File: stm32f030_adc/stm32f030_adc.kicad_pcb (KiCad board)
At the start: 2 copper layers, 38 parts, among them Q1 BC337, U1 STM32F103C6Tx, U2 AMS1117-3.3, X1 USB_B_Micro, Y2 8 MHz

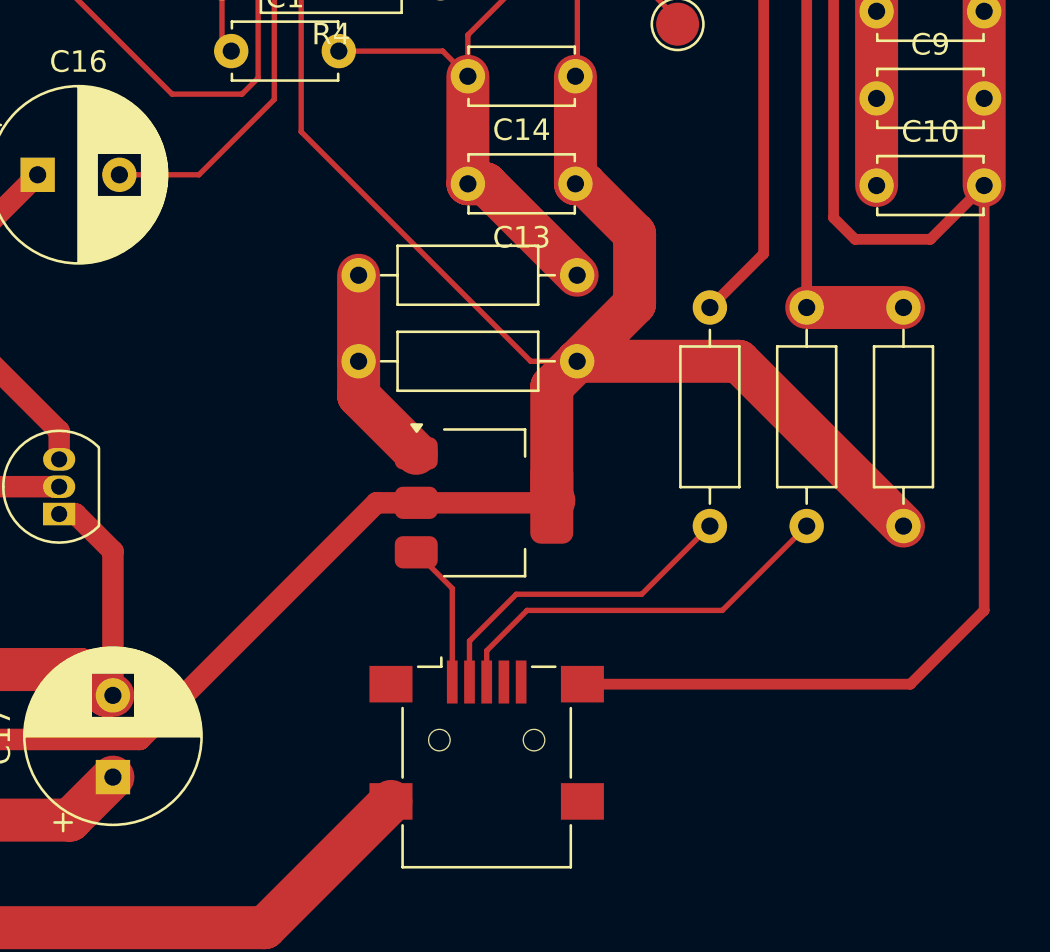
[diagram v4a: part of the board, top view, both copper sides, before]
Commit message: Layout: fixed unconnected items (except for the LDO which should not have the connection anyway)
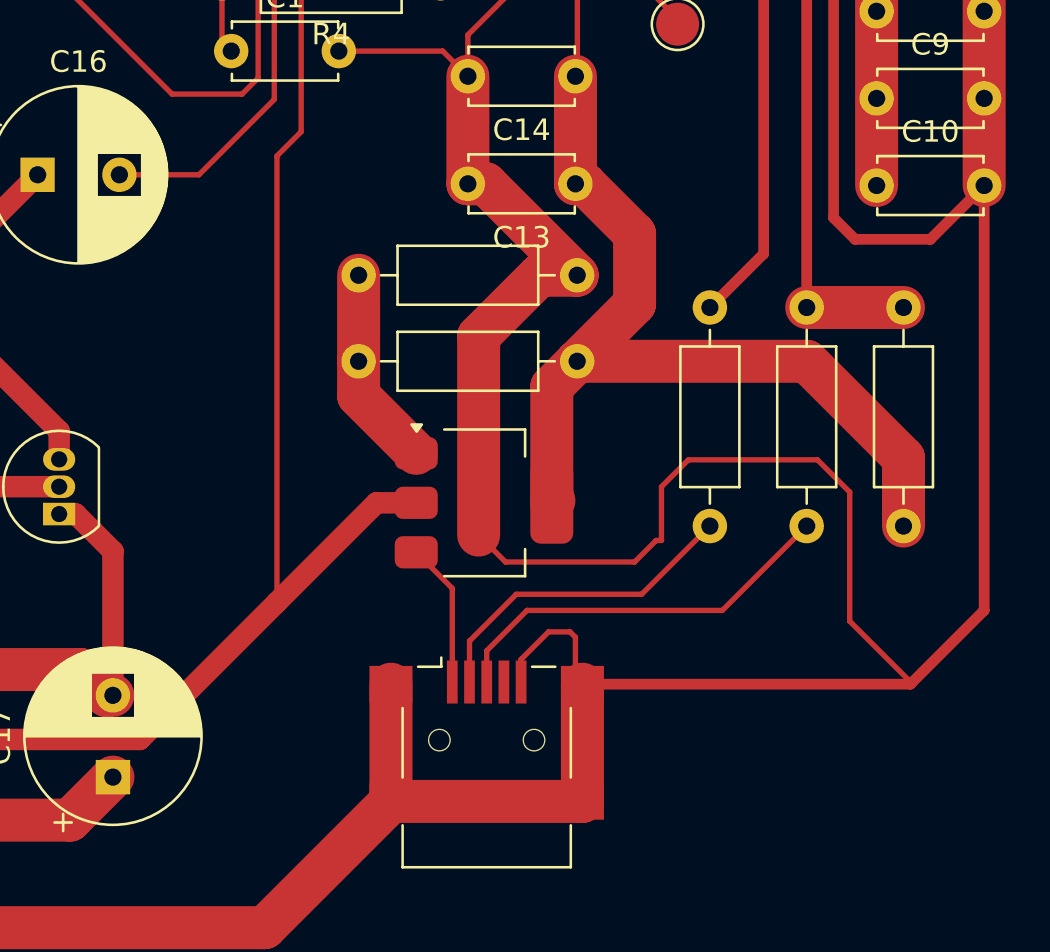
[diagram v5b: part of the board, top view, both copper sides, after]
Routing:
- net GNDREF: track 342.0 -> 415.2 mm
- net +3V3: track 221.2 -> 221.9 mm
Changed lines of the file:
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@@
 	)
 	(segment
-		(start 175.25 129.25)
-		(end 171.82 132.68)
-		(width 0.5)
+		(start 152.08 109.42)
+		(end 156.33 113.67)
+		(width 2)
 		(layer "F.Cu")
 		(net 1)
@@
 	)
 	(segment
+		(start 147.675 138.13)
+		(end 147.675 132.68)
+		(width 2)
+		(layer "F.Cu")
+		(net 1)
+	)
+	(segment
 		(start 117.552651 85.5)
 		(end 129 85.5)
@@
 	)
 	(segment
+		(start 147.675 138.13)
+		(end 156.575 138.13)
+		(width 2)
+		(layer "F.Cu")
+		(net 1)
+	)
+	(segment
 		(start 129 85.5)
 		(end 133 89.5)
@@
 	)
 	(segment
+		(start 159 127)
+		(end 160 126)
+		(width 0.25)
+		(layer "F.Cu")
+		(net 1)
+	)
+	(segment
 		(start 175.25 109.5)
 		(end 175.25 129.25)
@@
 	)
 	(segment
+		(start 169 129.75)
+		(end 171.875 132.625)
+		(width 0.25)
+		(layer "F.Cu")
+		(net 1)
+	)
+	(segment
 		(start 137.5 105.25)
 		(end 140.75 105.25)
@@
 	)
 	(segment
+		(start 160.25 126)
+		(end 160.25 123.5)
+		(width 0.25)
+		(layer "F.Cu")
+		(net 1)
+	)
+	(segment
+		(start 153.725 131.525)
+		(end 155 130.25)
+		(width 0.25)
+		(layer "F.Cu")
+		(net 1)
+	)
+	(segment
 		(start 141.5 104.5)
 		(end 141.5 98.5)
@@
 	)
 	(segment
+		(start 151.75 125.75)
+		(end 153 127)
+		(width 0.25)
+		(layer "F.Cu")
+		(net 1)
+	)
+	(segment
+		(start 153 127)
+		(end 159 127)
+		(width 0.25)
+		(layer "F.Cu")
+		(net 1)
+	)
+	(segment
+		(start 155 130.25)
+		(end 156 130.25)
+		(width 0.25)
+		(layer "F.Cu")
+		(net 1)
+	)
+	(segment
+		(start 151.25 109.42)
+		(end 152.08 109.42)
+		(width 2)
+		(layer "F.Cu")
+		(net 1)
+	)
+	(segment
 		(start 164.25 68.75)
 		(end 173.75 68.75)
@@
 	)
 	(segment
+		(start 171.875 132.625)
+		(end 171.82 132.68)
+		(width 0.5)
+		(layer "F.Cu")
+		(net 1)
+	)
+	(segment
+		(start 156.25 132.355)
+		(end 156.575 132.68)
+		(width 0.25)
+		(layer "F.Cu")
+		(net 1)
+	)
+	(segment
 		(start 114.17 125.92)
 		(end 110 121.75)
@@
 	)
 	(segment
+		(start 156.575 138.13)
+		(end 156.575 132.68)
+		(width 2)
+		(layer "F.Cu")
+		(net 1)
+	)
+	(segment
+		(start 169 123.75)
+		(end 169 129.75)
+		(width 0.25)
+		(layer "F.Cu")
+		(net 1)
+	)
+	(segment
 		(start 163 87.5)
 		(end 166.25 87.5)
@@
 	)
 	(segment
+		(start 154.58 113.67)
+		(end 151.75 116.5)
+		(width 2)
+		(layer "F.Cu")
+		(net 1)
+	)
+	(segment
 		(start 157.75 90.25)
 		(end 160.25 90.25)
@@
 	)
 	(segment
+		(start 156.25 130.5)
+		(end 156.25 132.355)
+		(width 0.25)
+		(layer "F.Cu")
+		(net 1)
+	)
+	(segment
 		(start 141.805 144)
 		(end 147.675 138.13)
@@
 	)
 	(segment
+		(start 156.33 113.67)
+		(end 154.58 113.67)
+		(width 2)
+		(layer "F.Cu")
+		(net 1)
+	)
+	(segment
 		(start 114.17 126)
 		(end 114.17 125.92)
@@
 	)
 	(segment
-		(start 151.25 109.42)
-		(end 152.08 109.42)
-		(width 2)
+		(start 160.25 123.5)
+		(end 161.5 122.25)
+		(width 0.25)
+		(layer "F.Cu")
+		(net 1)
+	)
+	(segment
+		(start 160 126)
+		(end 160.25 126)
+		(width 0.25)
 		(layer "F.Cu")
 		(net 1)
@@
 	)
 	(segment
+		(start 175.25 129.25)
+		(end 171.875 132.625)
+		(width 0.5)
+		(layer "F.Cu")
+		(net 1)
+	)
+	(segment
 		(start 114.17 139)
 		(end 114.17 142.117349)
@@
 	)
 	(segment
+		(start 153.725 132.58)
+		(end 153.725 131.525)
+		(width 0.25)
+		(layer "F.Cu")
+		(net 1)
+	)
+	(segment
 		(start 169.25 112)
 		(end 172.75 112)
@@
 	)
 	(segment
+		(start 161.5 122.25)
+		(end 167.5 122.25)
+		(width 0.25)
+		(layer "F.Cu")
+		(net 1)
+	)
+	(segment
 		(start 140.75 105.25)
 		(end 141.5 104.5)
@@
 	)
 	(segment
+		(start 151.75 116.5)
+		(end 151.75 125.75)
+		(width 2)
+		(layer "F.Cu")
+		(net 1)
+	)
+	(segment
 		(start 141.5 98.5)
 		(end 142.75 97.25)
@@
 	)
 	(segment
+		(start 167.5 122.25)
+		(end 169 123.75)
+		(width 0.25)
+		(layer "F.Cu")
+		(net 1)
+	)
+	(segment
+		(start 156 130.25)
+		(end 156.25 130.5)
+		(width 0.25)
+		(layer "F.Cu")
+		(net 1)
+	)
+	(segment
 		(start 175.33 70.33)
 		(end 175.33 72.75)
@@
 	)
 	(segment
-		(start 152.08 109.42)
-		(end 156.33 113.67)
-		(width 2)
-		(layer "F.Cu")
-		(net 1)
-	)
-	(segment
 		(start 149.425 92.75)
 		(end 148 92.75)
@@
 	)
 	(segment
-		(start 156.33 117.67)
-		(end 155.15 118.85)
-		(width 2)
-		(layer "F.Cu")
-		(net 3)
-	)
-	(segment
-		(start 154.17 117.67)
-		(end 156.33 117.67)
+		(start 144.15 100.1)
+		(end 143.5 100.75)
 		(width 0.25)
 		(layer "F.Cu")
@@
 	)
 	(segment
+		(start 171.5 122.165)
+		(end 167.005 117.67)
+		(width 2)
+		(layer "F.Cu")
+		(net 3)
+	)
+	(segment
+		(start 167.005 117.67)
+		(end 156.33 117.67)
+		(width 2)
+		(layer "F.Cu")
+		(net 3)
+	)
+	(segment
 		(start 114.17 119.42)
 		(end 114.09 119.5)
 		(width 2)
-		(layer "F.Cu")
-		(net 3)
-	)
-	(segment
-		(start 149.98 100.1)
-		(end 144.15 100.1)
-		(width 0.25)
 		(layer "F.Cu")
 		(net 3)
@@
 	)
 	(segment
-		(start 143.5 100.75)
-		(end 143.5 107)
-		(width 0.25)
-		(layer "F.Cu")
-		(net 3)
-	)
-	(segment
-		(start 171.5 125.33)
-		(end 163.84 117.67)
-		(width 2)
+		(start 147 124.25)
+		(end 142.375 128.875)
+		(width 1)
 		(layer "F.Cu")
 		(net 3)
@@
 	)
 	(segment
+		(start 142.375 108.125)
+		(end 142.375 128.875)
+		(width 0.25)
+		(layer "F.Cu")
+		(net 3)
+	)
+	(segment
 		(start 156.25 104.42)
 		(end 156.25 109.42)
@@
 	)
 	(segment
-		(start 163.84 117.67)
-		(end 156.33 117.67)
-		(width 2)
-		(layer "F.Cu")
-		(net 3)
-	)
-	(segment
 		(start 120.25 124.75)
 		(end 120.25 134)
@@
 	)
 	(segment
+		(start 171.5 125.33)
+		(end 171.5 122.165)
+		(width 2)
+		(layer "F.Cu")
+		(net 3)
+	)
+	(segment
+		(start 143.5 107)
+		(end 142.375 108.125)
+		(width 0.25)
+		(layer "F.Cu")
+		(net 3)
+	)
+	(segment
+		(start 142.375 128.875)
+		(end 136 135.25)
+		(width 1)
+		(layer "F.Cu")
+		(net 3)
+	)
+	(segment
 		(start 170.25 109.5)
 		(end 170.25 77.1)
@@
 	)
 	(segment
-		(start 143.5 107)
-		(end 154.17 117.67)
-		(width 0.25)
-		(layer "F.Cu")
-		(net 3)
-	)
-	(segment
 		(start 156.3375 90)
 		(end 156.5875 89.75)
@@
 	)
 	(segment
+		(start 143.5 100.75)
+		(end 143.5 107)
+		(width 0.25)
+		(layer "F.Cu")
+		(net 3)
+	)
+	(segment
 		(start 121.5 135.25)
 		(end 127 135.25)
@@
 	)
 	(segment
-		(start 147 124.25)
-		(end 136 135.25)
-		(width 1)
+		(start 149.98 100.1)
+		(end 144.15 100.1)
+		(width 0.25)
 		(layer "F.Cu")
 		(net 3)
@@
 	)
 	(segment
-		(start 148.85 124.25)
-		(end 155.15 124.25)
-		(width 1)
-		(layer "F.Cu")
-		(net 3)
-	)
-	(segment
 		(start 150.8375 89.75)
 		(end 150.8375 88.3375)
@@
 	)
 	(segment
-		(start 144.15 100.1)
-		(end 143.5 100.75)
-		(width 0.25)
-		(layer "F.Cu")
-		(net 3)
+		(start 155.15 118.85)
+		(end 156.33 117.67)
+		(width 2)
+		(layer "F.Cu")
+		(net 3)

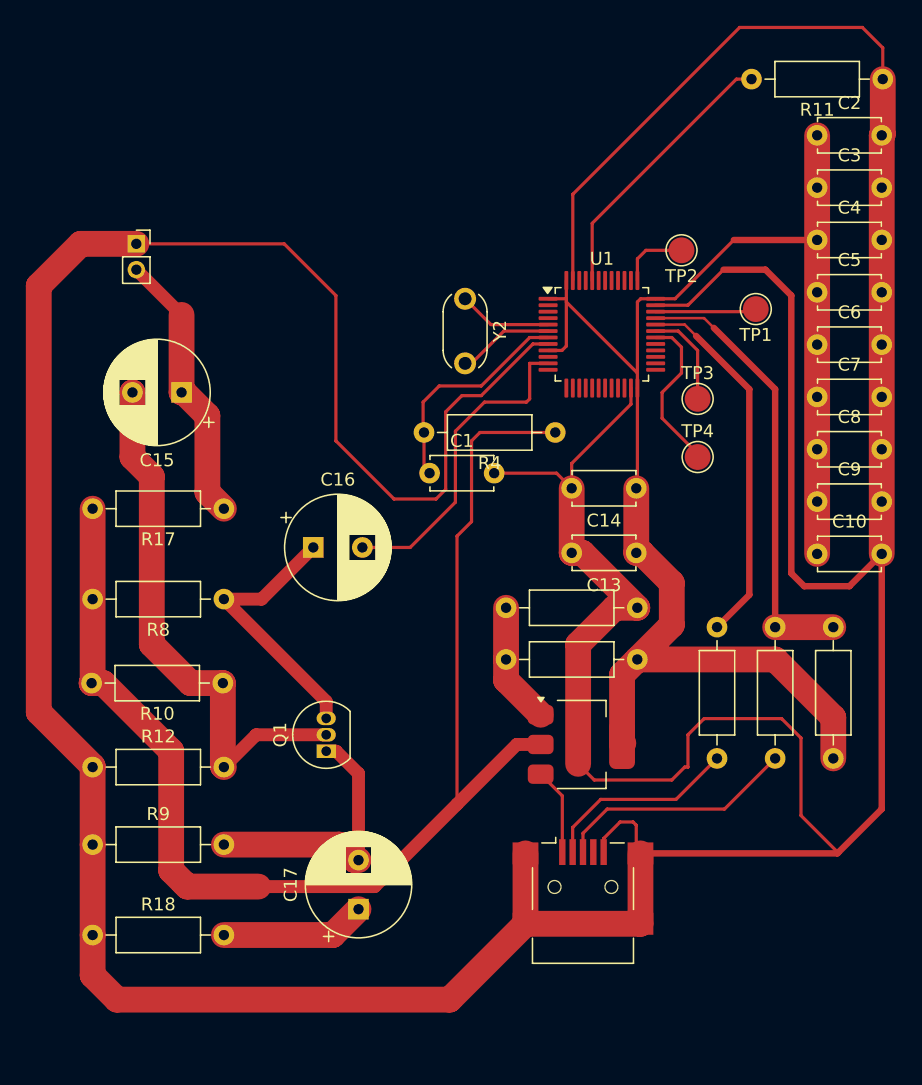
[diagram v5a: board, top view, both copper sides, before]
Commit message: Layout: GNDREF at the perimeter of the board:x
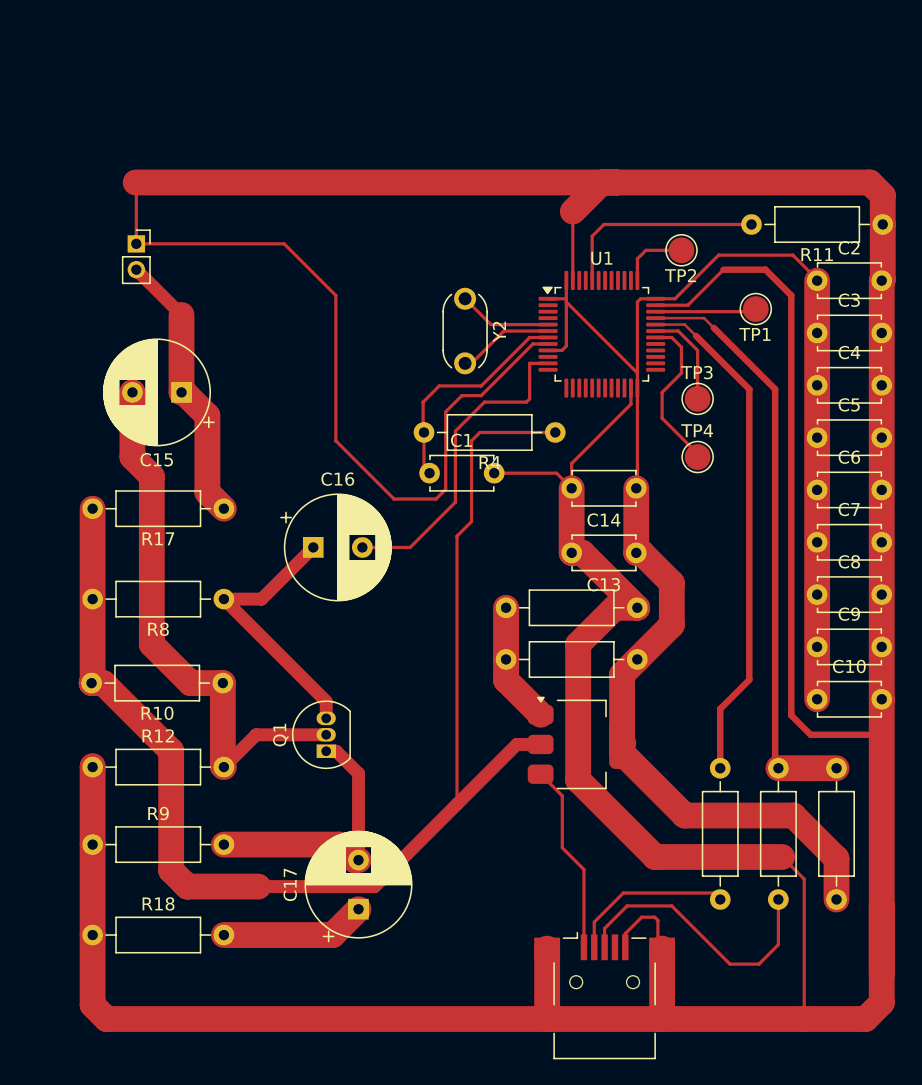
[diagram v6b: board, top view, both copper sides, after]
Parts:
- moved C10 11.2 mm to (170.2, 120.8)
- moved C2 11.2 mm to (170.2, 88.3)
- moved C3 11.2 mm to (170.2, 92.4)
- moved C4 11.2 mm to (170.2, 96.5)
- moved C5 11.2 mm to (170.2, 100.5)
- moved C6 11.2 mm to (170.2, 104.5)
- moved C7 11.2 mm to (170.2, 108.6)
- moved C8 11.2 mm to (170.2, 112.7)
- moved C9 11.2 mm to (170.2, 116.7)
- moved R11 11.2 mm to (175.3, 84.0)
- moved R5 10.9 mm to (167.2, 136.2)
- moved R6 10.9 mm to (162.8, 136.2)
- moved R7 10.9 mm to (171.8, 126.1)
- moved X1 7.56 mm to (153.8, 142.7)
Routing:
- net /Power and MCU/USB_D+: track 34.4 -> 45.5 mm
- net /Power and MCU/USB_D-: track 28.8 -> 39.6 mm
- net 5V_USB: track 6.72 -> 14.8 mm
- net GNDREF: track 415.2 -> 421.7 mm
- net Net-(U1-BOOT0): track 21.4 -> 16.1 mm
- net +3V3: track 221.9 -> 225.9 mm
- net Net-(X1-D+): track 18.7 -> 21.6 mm
- net Net-(X1-D-): track 15.3 -> 12.8 mm

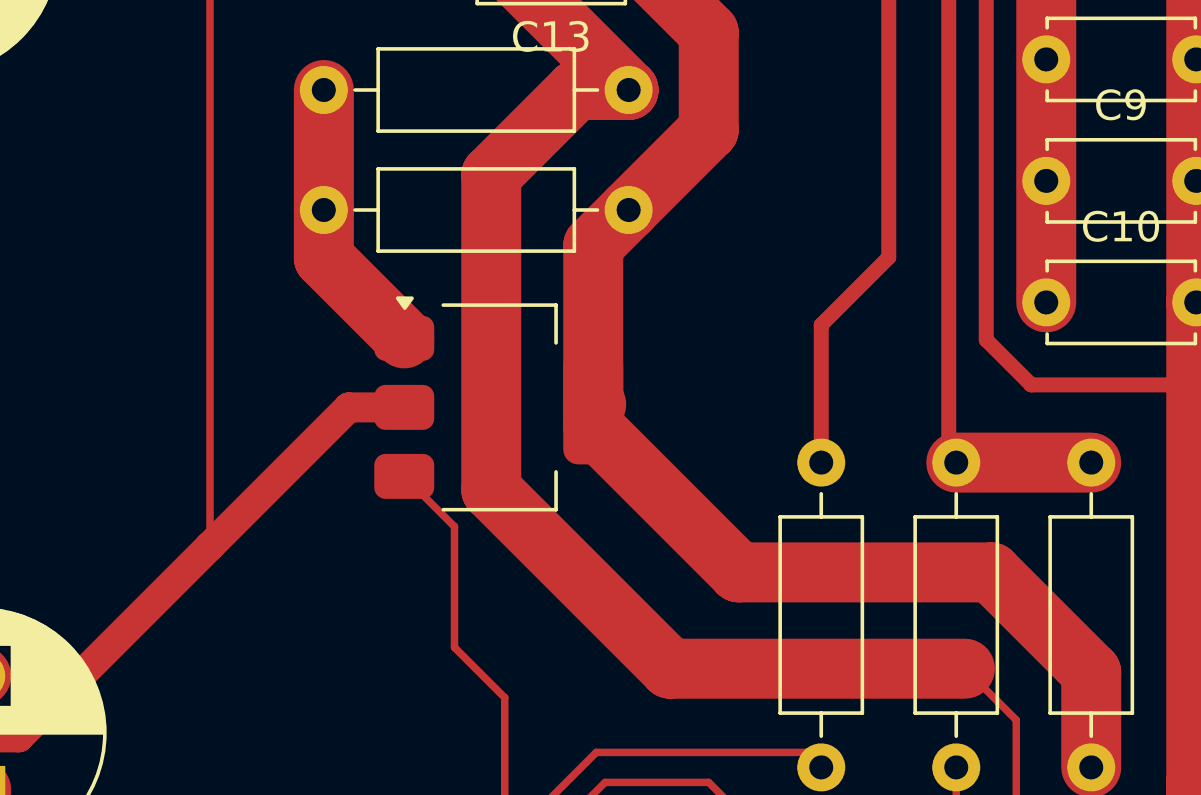
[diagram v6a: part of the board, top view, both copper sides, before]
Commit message: Furhter fixes: added jumper for 3V3
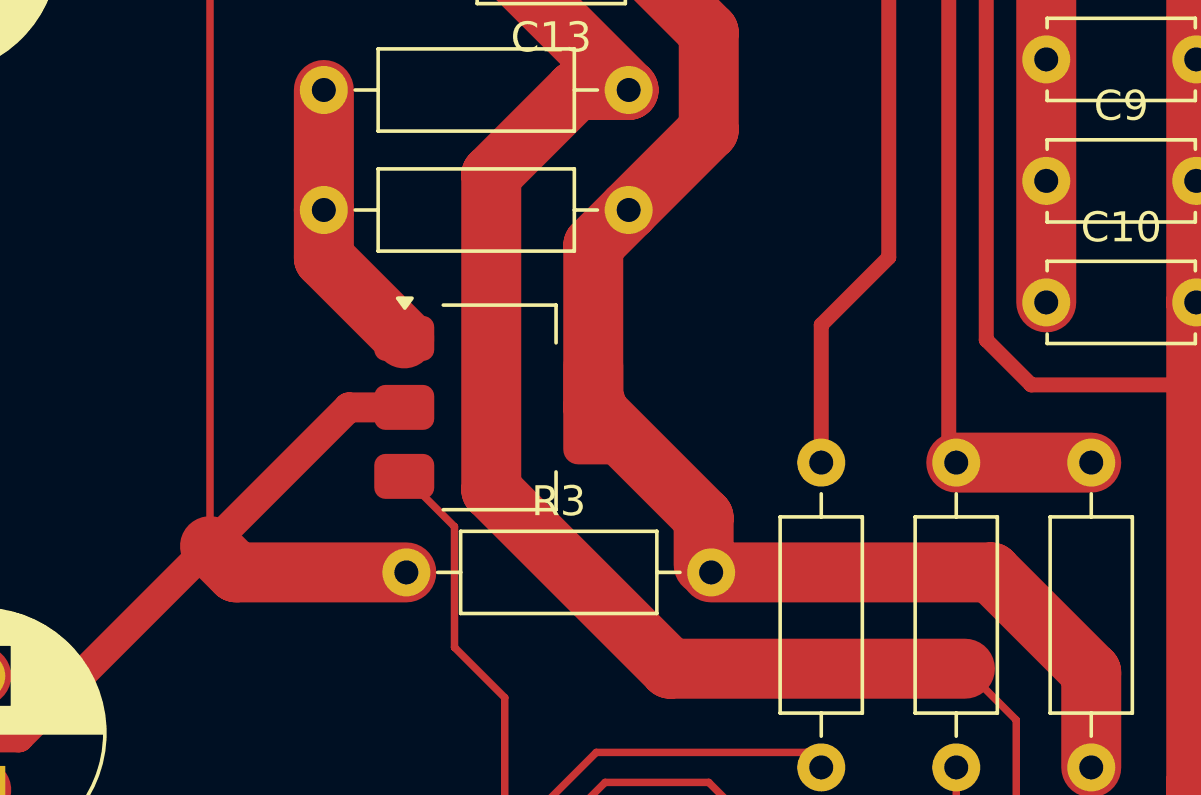
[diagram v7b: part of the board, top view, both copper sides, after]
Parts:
- added R3: 0, Resistor_THT:R_Axial_DIN0207_L6.3mm_D2.5mm_P10.16mm_Horizontal, F.Cu at (148.9, 129.8)
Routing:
- net +3V3: track 225.9 -> 232.9 mm
